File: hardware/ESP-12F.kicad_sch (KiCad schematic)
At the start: 22 parts, among them U5 ESP-12F, U7 PI4IOE5V6416LEX, U8 PI4IOE5V6416LEX, U9 MCP2558FD-xMF

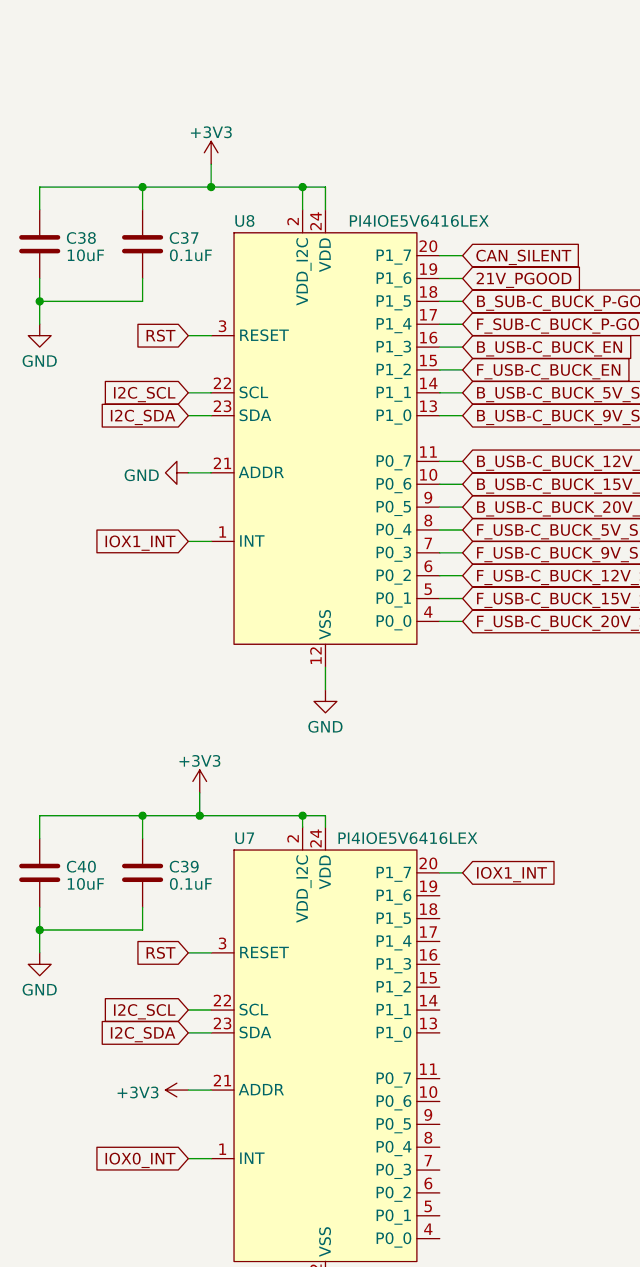
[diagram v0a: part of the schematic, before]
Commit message: working on io_call and auto init for pins
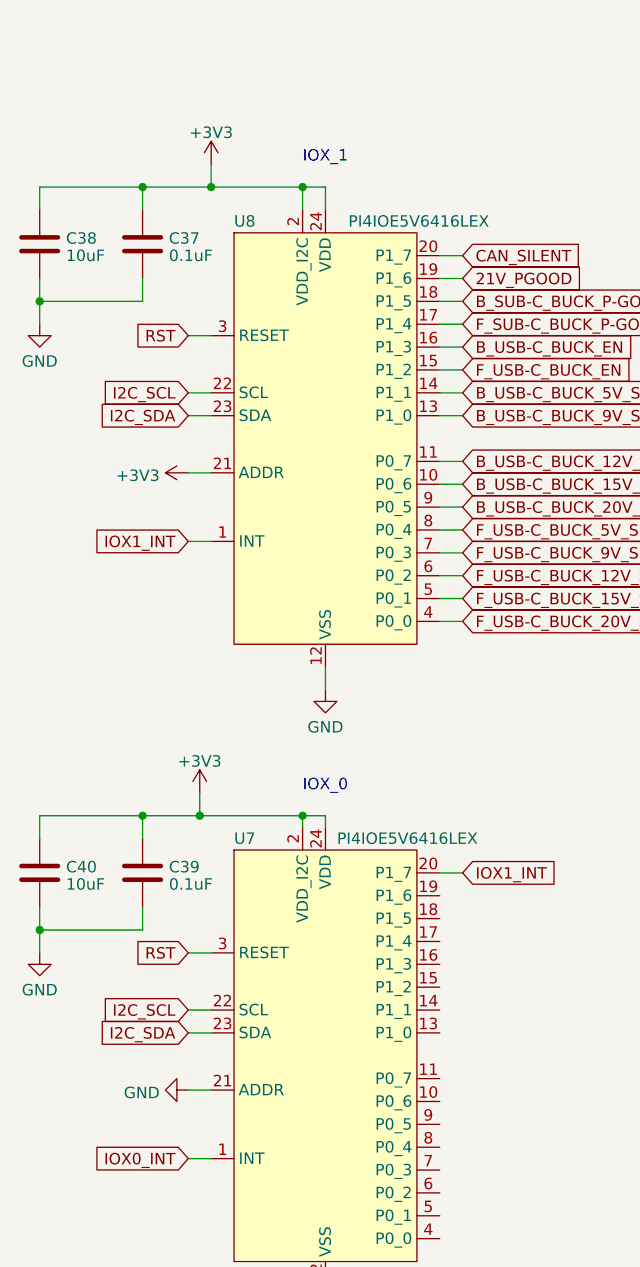
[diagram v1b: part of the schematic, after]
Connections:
- net +3V3: now also U8.21 (ADDR); no longer U7.21 (ADDR)
- net GND: now also U7.21 (ADDR); no longer U8.21 (ADDR)
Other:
- note added: "IOX_0"
- note added: "IOX_1"
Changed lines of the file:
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@@
     (stroke (width 0) (type default))
   )
+  (text "IOX_0" (at 67.31 110.49 0)
+    (effects (font (size 1.27 1.27)) (justify left bottom))
+  )
+  (text "IOX_1" (at 67.31 40.64 0)
+    (effects (font (size 1.27 1.27)) (justify left bottom))
+  )
   (global_label "B_SUB-C_BUCK_P-GOOD" (shape input) (at 85.09 55.88 0) (fields_autoplaced)
     (effects (font (size 1.27 1.27)) (justify left))
@@
     )
   )
-  (symbol (lib_id "power:GND") (at 54.61 74.93 270) (unit 1)
-    (in_bom yes) (on_board yes) (dnp no) (fields_autoplaced)
-    (property "Reference" "#PWR037" (at 48.26 74.93 0)
-      (effects (font (size 1.27 1.27)) hide)
-    )
-    (property "Value" "GND" (at 51.4351 75.2468 90)
+  (symbol (lib_id "power:GND") (at 54.61 143.51 270) (unit 1)
+    (in_bom yes) (on_board yes) (dnp no) (fields_autoplaced)
+    (property "Reference" "#PWR037" (at 48.26 143.51 0)
+      (effects (font (size 1.27 1.27)) hide)
+    )
+    (property "Value" "GND" (at 51.4351 143.8268 90)
       (effects (font (size 1.27 1.27)) (justify right))
     )
-    (property "Footprint" "" (at 54.61 74.93 0)
-      (effects (font (size 1.27 1.27)) hide)
-    )
-    (property "Datasheet" "" (at 54.61 74.93 0)
+    (property "Footprint" "" (at 54.61 143.51 0)
+      (effects (font (size 1.27 1.27)) hide)
+    )
+    (property "Datasheet" "" (at 54.61 143.51 0)
       (effects (font (size 1.27 1.27)) hide)
     )
@@
     )
   )
-  (symbol (lib_id "power:+3V3") (at 54.61 143.51 90) (unit 1)
-    (in_bom yes) (on_board yes) (dnp no) (fields_autoplaced)
-    (property "Reference" "#PWR038" (at 58.42 143.51 0)
-      (effects (font (size 1.27 1.27)) hide)
-    )
-    (property "Value" "+3V3" (at 51.435 143.8268 90)
-      (effects (font (size 1.27 1.27)) (justify left))
-    )
-    (property "Footprint" "" (at 54.61 143.51 0)
-      (effects (font (size 1.27 1.27)) hide)
-    )
-    (property "Datasheet" "" (at 54.61 143.51 0)
-      (effects (font (size 1.27 1.27)) hide)
-    )
+  (symbol (lib_id "power:+3V3") (at 54.61 74.93 90) (unit 1)
+    (in_bom yes) (on_board yes) (dnp no) (fields_autoplaced)
+    (property "Reference" "#PWR038" (at 58.42 74.93 0)
+      (effects (font (size 1.27 1.27)) hide)
+    )
+    (property "Value" "+3V3" (at 51.435 75.2468 90)
+      (effects (font (size 1.27 1.27)) (justify left))
+    )
+    (property "Footprint" "" (at 54.61 74.93 0)
+      (effects (font (size 1.27 1.27)) hide)
+    )
+    (property "Datasheet" "" (at 54.61 74.93 0)
+      (effects (font (size 1.27 1.27)) hide)
+    )

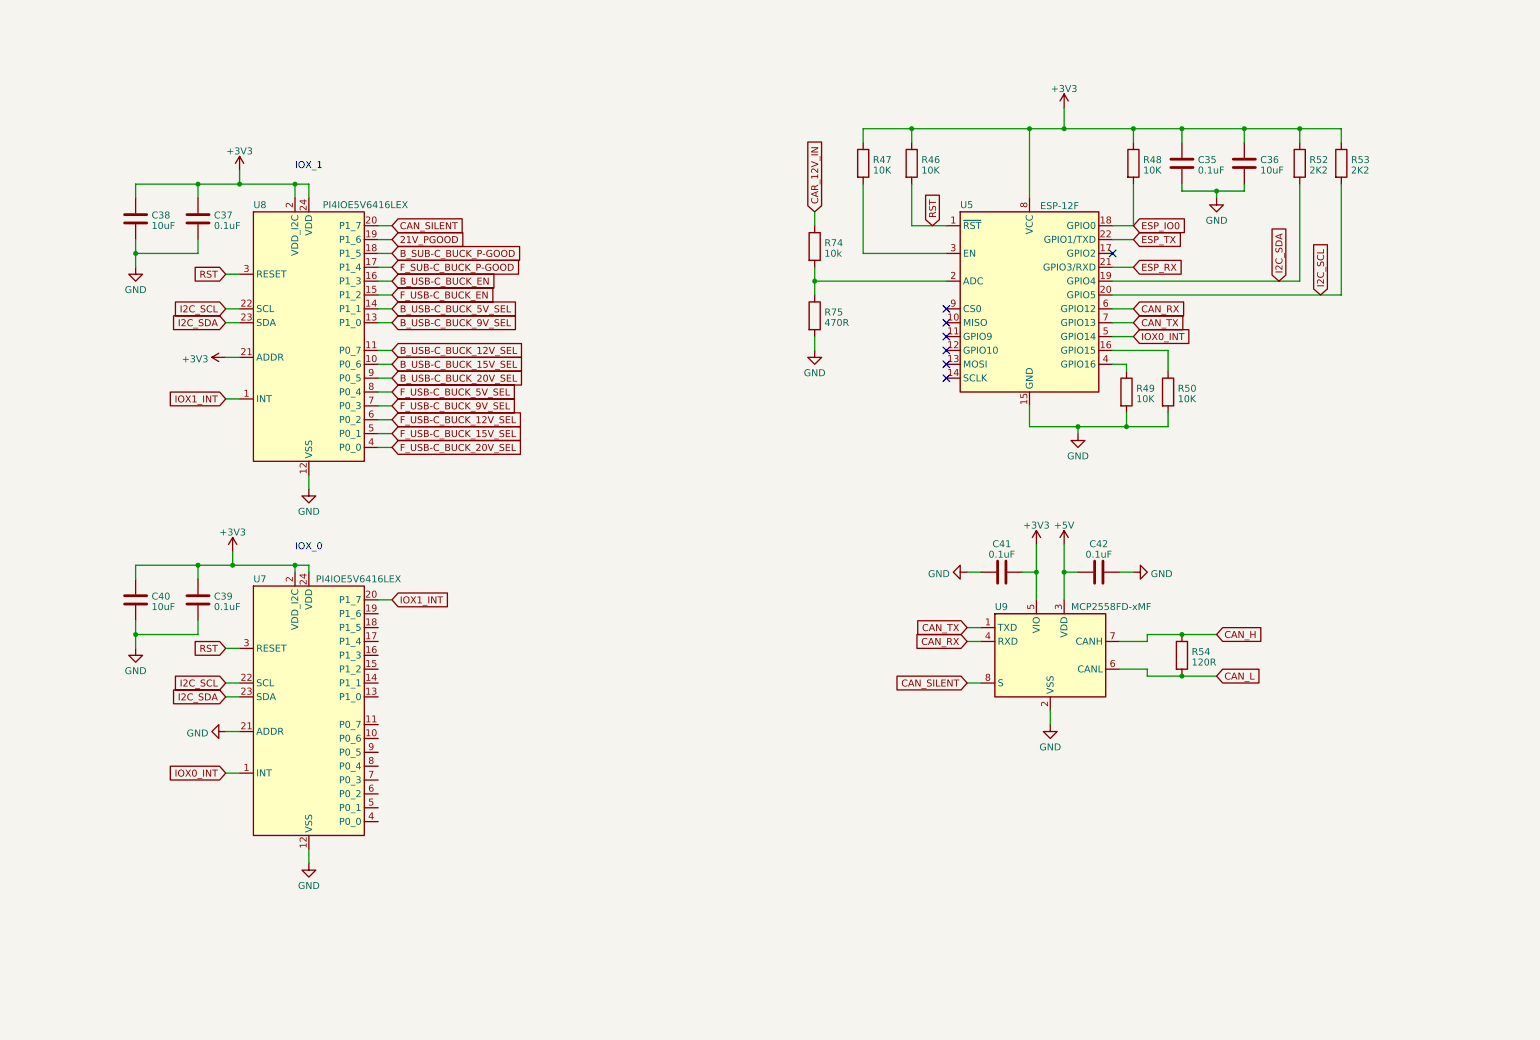
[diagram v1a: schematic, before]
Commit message: working on hardware agin as well as implimentded auto adc init and read
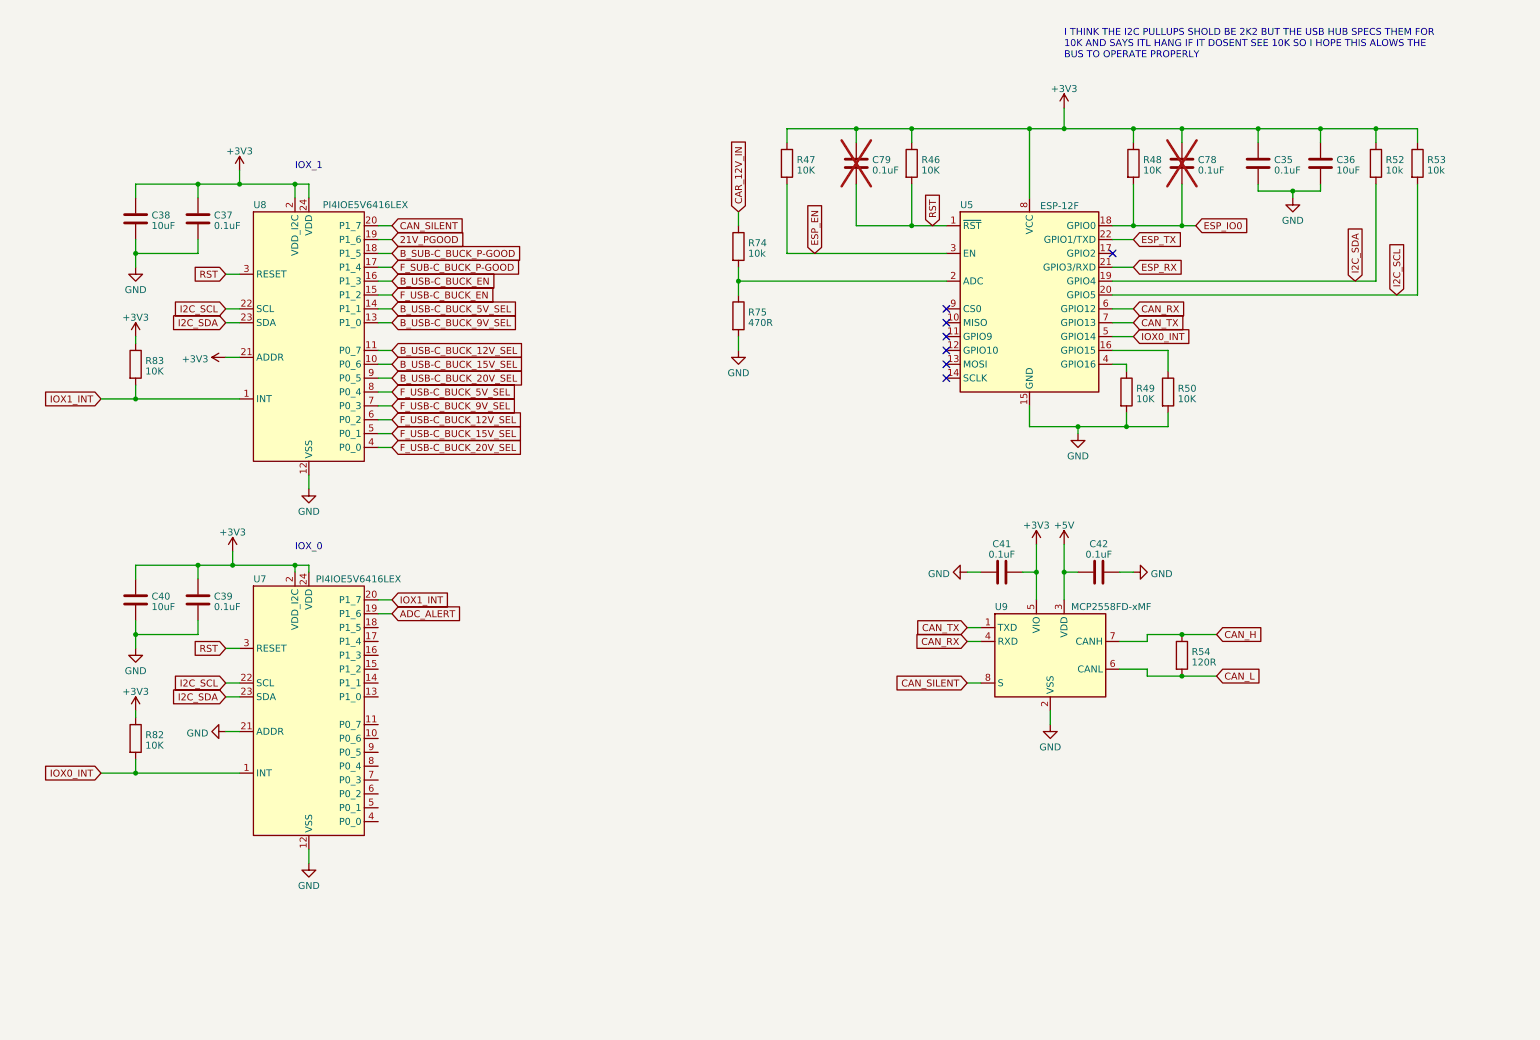
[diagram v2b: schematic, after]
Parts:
- added C78, C79: 0.1uF, symbol Device:C
- added R82, R83: 10K, symbol Device:R
- R52, R53: value 2K2 -> 10k
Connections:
- net +3V3: now also C78.1, C79.1, R82.1, R83.1
- net ESP_IO0: now also C78.2
- net IOX0_INT: now also R82.2
- net IOX1_INT: now also R83.2
- net RST: now also C79.2
- net ADC_ALERT: now reaches U7.19 (P1_6)
- net ESP_EN: now reaches R47.2, U5.3 (EN)
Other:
- note added: "I THINK THE I2C PULLUPS SHOLD BE 2K2 BUT THE USB HUB SPECS THEM FOR 10K AND SAYS ITL HANG IF IT DOSENT SEE 10K SO I HOPE THIS ALOWS THE BUS TO OPERATE PROPERLY"
- moved on the sheet: C35, C36, R47, R52, R53, R74, R75

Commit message: finnished rudimentry schimatics still needs alot of work
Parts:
- added JP15: ~, symbol Jumper:SolderJumper_2_Open
- added JP16, JP17: ~, symbol Jumper:SolderJumper_3_Open
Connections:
- net CAN_H: now also JP15.2 (B); no longer R54.1
- net I2C_SCL: now also JP17.1 (A)
- net I2C_SDA: now also JP16.1 (A)
- net SRC_BTN: now reaches U7.13 (P1_0)
- net UNIT_BTN: now reaches U7.14 (P1_1)
- net DISP_IRQ: now reaches U7.15 (P1_2)
- net DFP_C_ATTACH_1: now reaches U7.16 (P1_3)
- net HUB_VBUS_DET: now reaches U7.17 (P1_4)
- net UFP_C_ATTACH_0: now reaches U7.18 (P1_5)
- net IOX_0_P_0_0: now reaches U7.4 (P0_0)
- net IOX_0_P_0_0: now also JP16.3 (B)
- net IOX_0_P_0_1: now reaches U7.5 (P0_1)
- net IOX_0_P_0_1: now also JP17.3 (B)
- new net: JP15.1 (A), R54.1
- new net DSUB_P_6: JP16.2 (C)
- new net DSUB_P_7: JP17.2 (C)
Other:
- moved on the sheet: R54

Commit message: working on hardware
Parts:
- C39: renamed from C38; footprint (none) -> Capacitor_SMD:C_0603_1608Metric
- C40: footprint (none) -> Capacitor_SMD:C_0603_1608Metric
- C41: renamed from C37; footprint (none) -> Capacitor_SMD:C_0603_1608Metric
- C42: renamed from C39; footprint (none) -> Capacitor_SMD:C_0603_1608Metric
- C43: renamed from C79; footprint (none) -> Capacitor_SMD:C_0603_1608Metric
- C44: renamed from C41; footprint (none) -> Capacitor_SMD:C_0603_1608Metric
- C45: renamed from C78; footprint (none) -> Capacitor_SMD:C_0603_1608Metric
- C46: renamed from C42; footprint (none) -> Capacitor_SMD:C_0603_1608Metric
- C47: renamed from C35; footprint (none) -> Capacitor_SMD:C_0603_1608Metric
- C48: renamed from C36; footprint (none) -> Capacitor_SMD:C_0603_1608Metric
- JP1: renamed from JP17; footprint (none) -> Jumper:SolderJumper-3_P1.3mm_Open_RoundedPad1.0x1.5mm_NumberLabels
- JP2: renamed from JP16; footprint (none) -> Jumper:SolderJumper-3_P1.3mm_Open_RoundedPad1.0x1.5mm_NumberLabels
- JP3: renamed from JP15; footprint (none) -> Jumper:SolderJumper-2_P1.3mm_Open_RoundedPad1.0x1.5mm
- renumbered R83 to R50, R82 to R51, R74 to R52, R75 to R53, R47 to R54, R46 to R55, R49 to R56, R48 to R57, R50 to R58, R54 to R59, R52 to R60, R53 to R61, U5 to U10, U9 to U11, U7 to U9
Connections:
- net MODE_BTN: now reaches U9.11 (P0_7)
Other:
- note added: "CAN BUS TRANCEVER"
- note added: "CAR CONNECTOR GPIO OR I2C SELSCTION JUMPERS"
- note added: "ESP-12F"
- note added: "IO EXPANDERS"
- moved on the sheet: C44, C46, JP1, JP2, JP3, R59, U11
